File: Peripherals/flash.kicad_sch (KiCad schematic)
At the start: 2 parts

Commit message: Reorganised repo
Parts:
- C20: value 100n -> (none); footprint Capacitor_SMD:C_0603_1608Metric -> (none)
- U7: value ~ -> (none); footprint Package_SO:SOIC-8_5.23x5.23mm_P1.27mm -> (none)
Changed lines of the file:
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@@
   (symbol (lib_id "power:+3.3V") (at 72.39 41.91 270) (unit 1)
     (in_bom yes) (on_board yes) (fields_autoplaced)
-    (property "Reference" "#PWR046" (id 0) (at 68.58 41.91 0)
+    (property "Reference" "#PWR?" (id 0) (at 68.58 41.91 0)
       (effects (font (size 1.27 1.27)) hide)
     )
-    (property "Value" "+3.3V" (id 1) (at 76.2 41.9099 90)
+    (property "Value" "" (id 1) (at 76.2 41.9099 90)
       (effects (font (size 1.27 1.27)) (justify left))
     )
@@
   (symbol (lib_id "power:GND") (at 54.61 49.53 0) (unit 1)
     (in_bom yes) (on_board yes) (fields_autoplaced)
-    (property "Reference" "#PWR045" (id 0) (at 54.61 55.88 0)
+    (property "Reference" "#PWR?" (id 0) (at 54.61 55.88 0)
       (effects (font (size 1.27 1.27)) hide)
     )
-    (property "Value" "GND" (id 1) (at 54.61 54.61 0))
+    (property "Value" "" (id 1) (at 54.61 54.61 0))
     (property "Footprint" "" (id 2) (at 54.61 49.53 0)
       (effects (font (size 1.27 1.27)) hide)
@@
   (symbol (lib_id "power:+3.3V") (at 87.63 35.56 0) (unit 1)
     (in_bom yes) (on_board yes) (fields_autoplaced)
-    (property "Reference" "#PWR047" (id 0) (at 87.63 39.37 0)
+    (property "Reference" "#PWR?" (id 0) (at 87.63 39.37 0)
       (effects (font (size 1.27 1.27)) hide)
     )
-    (property "Value" "+3.3V" (id 1) (at 87.63 30.48 0))
+    (property "Value" "" (id 1) (at 87.63 30.48 0))
     (property "Footprint" "" (id 2) (at 87.63 35.56 0)
       (effects (font (size 1.27 1.27)) hide)
@@
       (effects (font (size 1.27 1.27)) (justify left))
     )
-    (property "Value" "100n" (id 1) (at 88.9 41.91 0)
+    (property "Value" "" (id 1) (at 88.9 41.91 0)
       (effects (font (size 1.27 1.27)) (justify left))
     )
-    (property "Footprint" "Capacitor_SMD:C_0603_1608Metric" (id 2) (at 88.5952 43.18 0)
+    (property "Footprint" "" (id 2) (at 88.5952 43.18 0)
       (effects (font (size 1.27 1.27)) hide)
     )
@@
       (effects (font (size 1.27 1.27)) (justify left))
     )
-    (property "Value" "~" (id 1) (at 56.6294 29.21 0)
+    (property "Value" "" (id 1) (at 56.6294 29.21 0)
       (effects (font (size 1.27 1.27)) (justify left))
     )
-    (property "Footprint" "Package_SO:SOIC-8_5.23x5.23mm_P1.27mm" (id 2) (at 54.61 39.37 0)
+    (property "Footprint" "" (id 2) (at 54.61 39.37 0)
       (effects (font (size 1.27 1.27)) hide)
     )
@@
   (symbol (lib_id "power:GND") (at 87.63 43.18 0) (unit 1)
     (in_bom yes) (on_board yes) (fields_autoplaced)
-    (property "Reference" "#PWR048" (id 0) (at 87.63 49.53 0)
+    (property "Reference" "#PWR?" (id 0) (at 87.63 49.53 0)
       (effects (font (size 1.27 1.27)) hide)
     )
-    (property "Value" "GND" (id 1) (at 87.63 48.26 0))
+    (property "Value" "" (id 1) (at 87.63 48.26 0))
     (property "Footprint" "" (id 2) (at 87.63 43.18 0)
       (effects (font (size 1.27 1.27)) hide)
@@
   (symbol (lib_id "power:+3.3V") (at 54.61 29.21 0) (unit 1)
     (in_bom yes) (on_board yes) (fields_autoplaced)
-    (property "Reference" "#PWR044" (id 0) (at 54.61 33.02 0)
+    (property "Reference" "#PWR?" (id 0) (at 54.61 33.02 0)
       (effects (font (size 1.27 1.27)) hide)
     )
-    (property "Value" "+3.3V" (id 1) (at 54.61 24.13 0))
+    (property "Value" "" (id 1) (at 54.61 24.13 0))
     (property "Footprint" "" (id 2) (at 54.61 29.21 0)
       (effects (font (size 1.27 1.27)) hide)

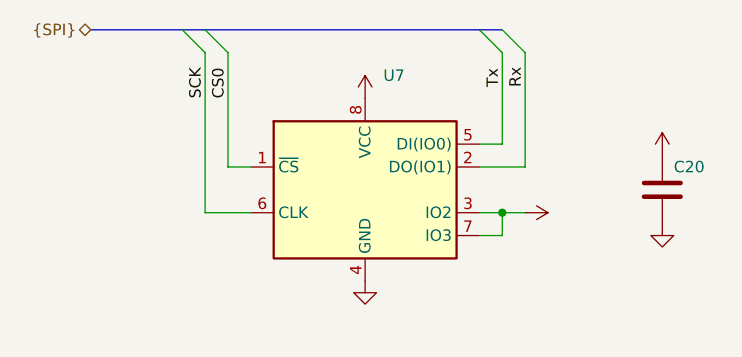
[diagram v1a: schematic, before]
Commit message: rev2 changes excluding pyro
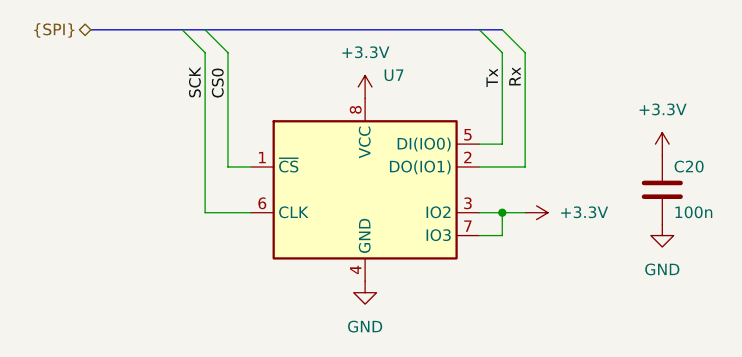
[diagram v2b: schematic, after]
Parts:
- C20: value (none) -> 100n; footprint (none) -> Capacitor_SMD:C_0603_1608Metric
- U7: value (none) -> ~; footprint (none) -> Package_SO:SOIC-8_5.23x5.23mm_P1.27mm
